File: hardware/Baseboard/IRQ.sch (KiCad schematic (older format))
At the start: 8 parts, among them IC11 74HC148, IC12 74HC273, SW4 NMI

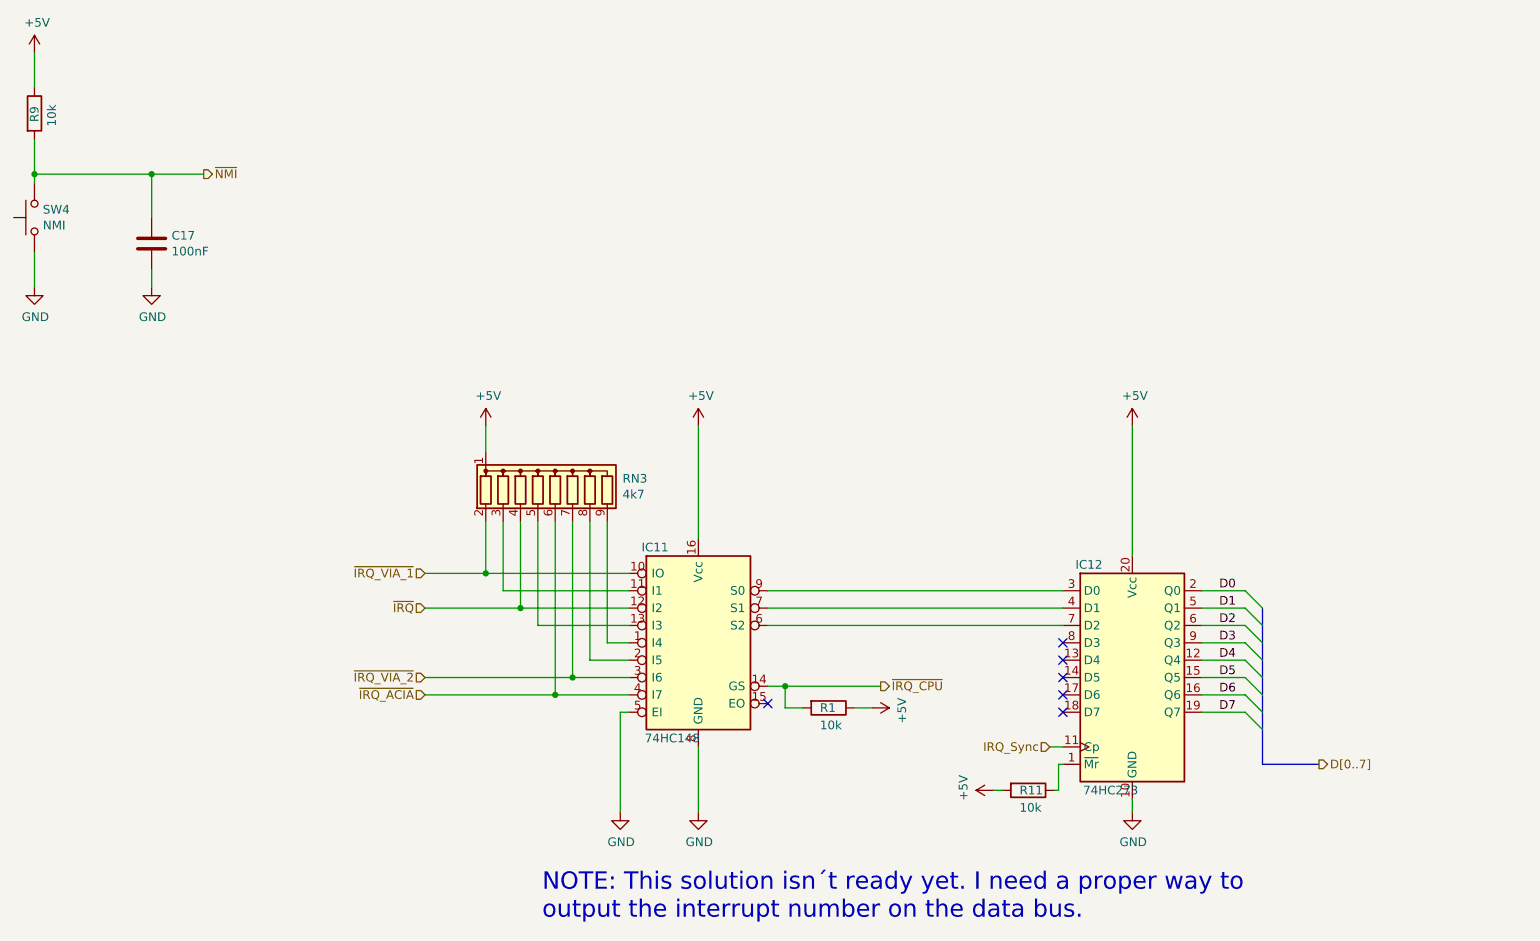
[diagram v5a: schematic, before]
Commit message: Add VP signal to expansion header, optimize routing
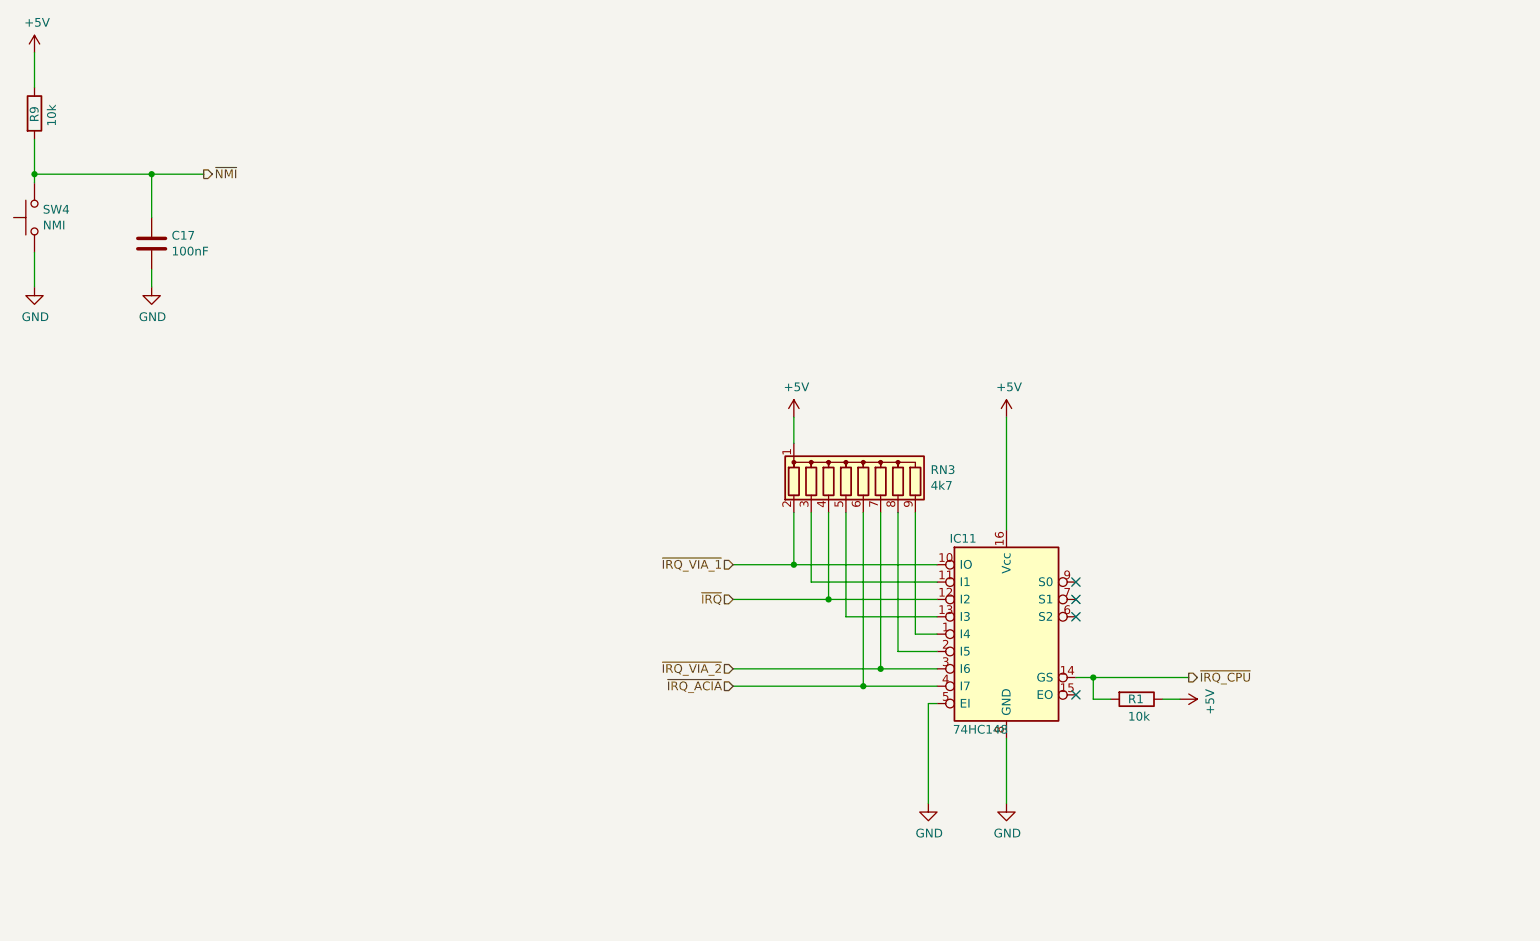
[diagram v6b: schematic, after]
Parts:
- removed IC12: 74HC273, Package_DIP:DIP-20_W7.62mm_LongPads, symbol Logic:74HC273
- removed R11: 10k, Resistor_THT:R_Axial_DIN0207_L6.3mm_D2.5mm_P7.62mm_Horizontal, symbol Device:R
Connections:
- no-connect marks 6 -> 4
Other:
- note removed: "NOTE: This solution isn´t ready yet. I need a proper way to\noutput the interrupt number on the data bus."
- moved on the sheet: IC11, R1, RN3
